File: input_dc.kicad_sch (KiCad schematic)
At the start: 24 parts

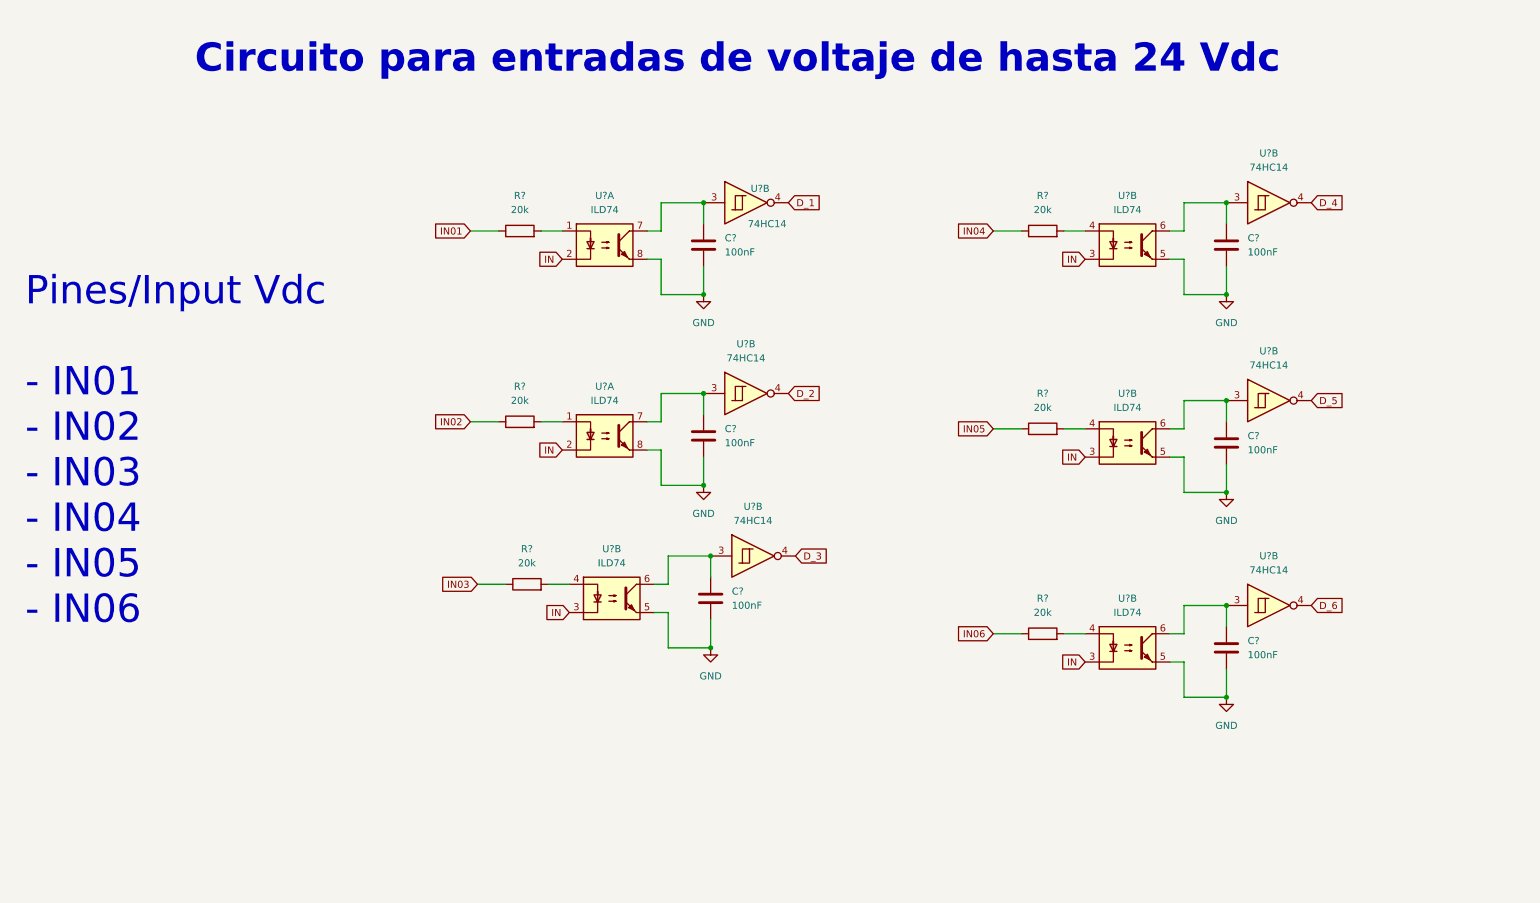
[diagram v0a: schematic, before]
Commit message: Esquema con comentarios
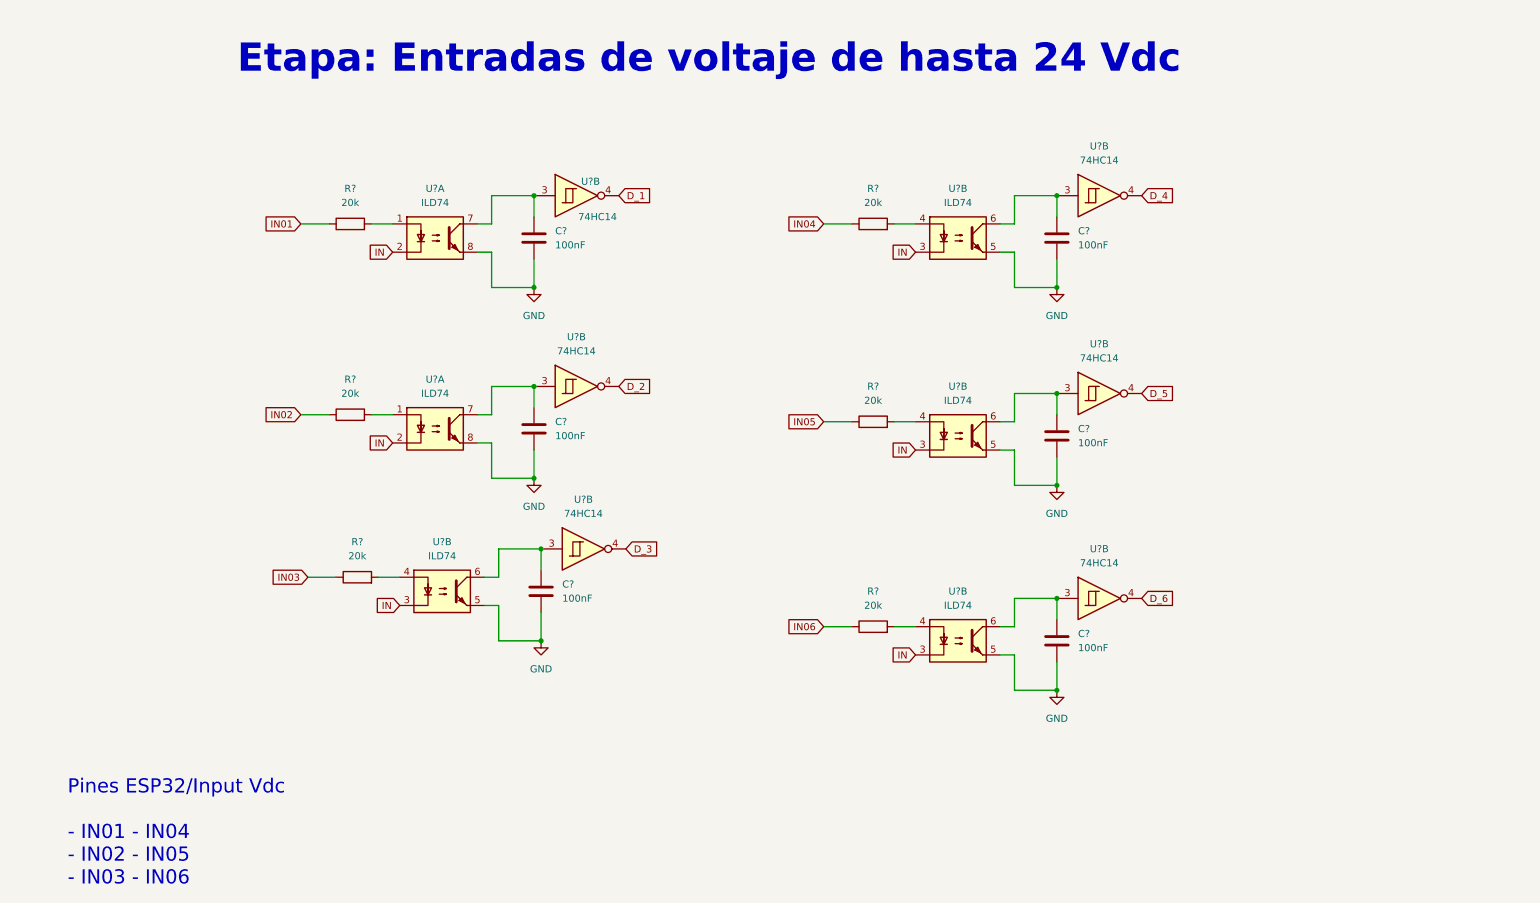
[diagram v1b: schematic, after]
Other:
- note added: "Etapa: Entradas de voltaje de hasta 24 Vdc"
- note added: "Pines ESP32/Input Vdc - IN01 - IN04 - IN02 - IN05 - IN03 - IN06"
- note removed: "Circuito para entradas de voltaje de hasta 24 Vdc"
- note removed: "Pines/Input Vdc - IN01 - IN02 - IN03 - IN04 - IN05 - IN06"
- moved on the sheet: C?, R?, U?A, U?B

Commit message: Documentación pines esp32
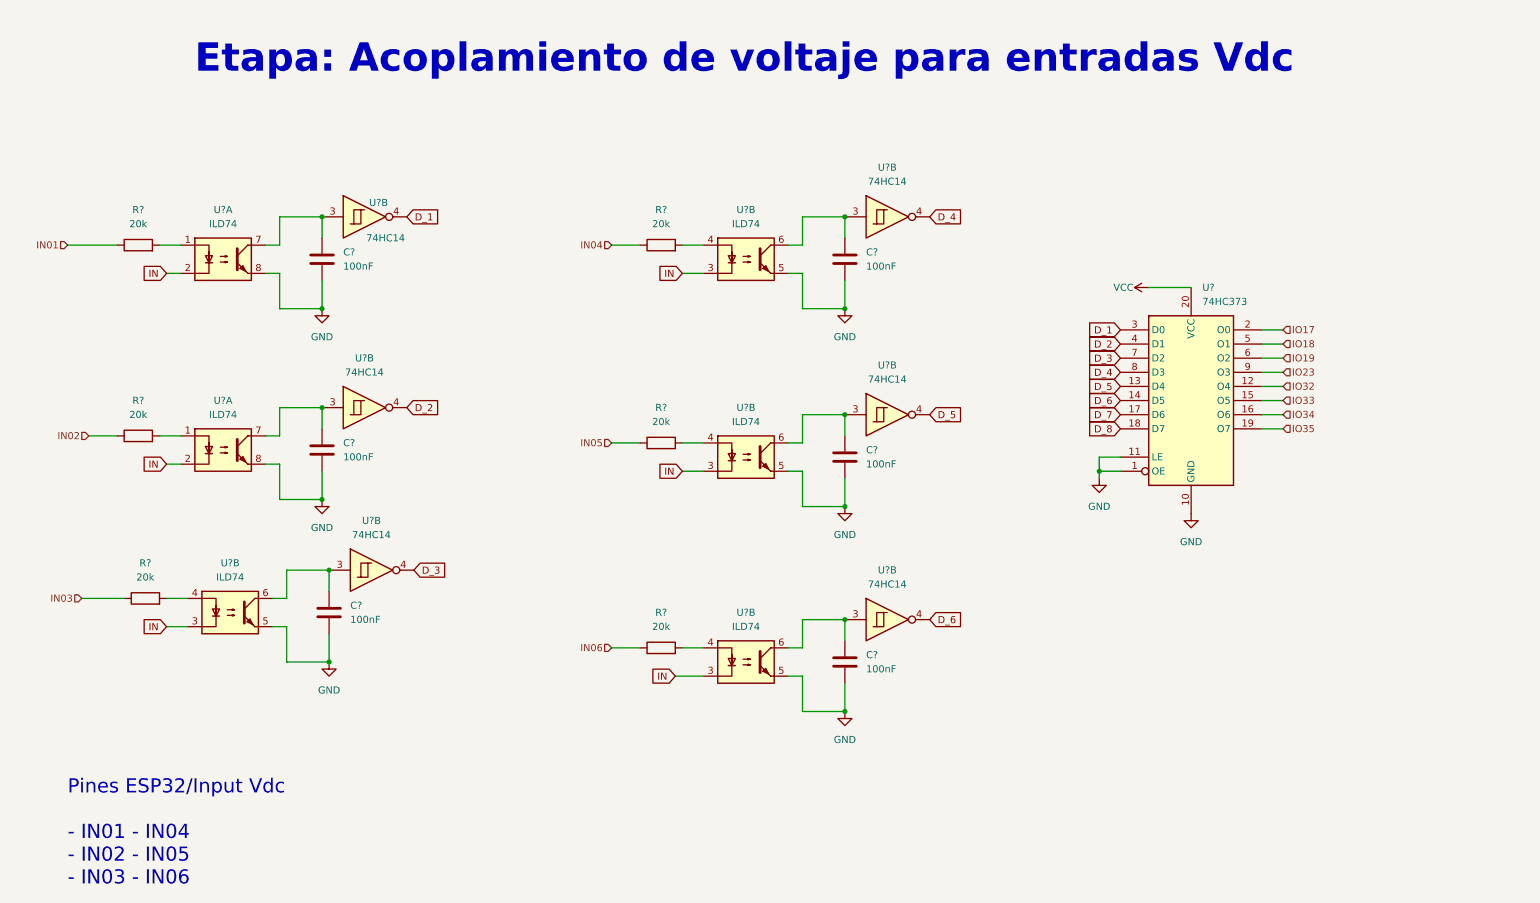
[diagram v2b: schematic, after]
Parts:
- added U?: 74HC373, Package_SO:SSOP-20_4.4x6.5mm_P0.65mm, symbol 74xx:74HC373
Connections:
- net D_1: now also U?.3 (D0)
- net D_2: now also U?.4 (D1)
- net D_3: now also U?.7 (D2)
- net D_4: now also U?.8 (D3)
- net D_5: now also U?.13 (D4)
- net D_6: now also U?.14 (D5)
- net GND: now also U?.1 (OE), U?.10 (GND), U?.11 (LE)
- new net D_7: U?.17 (D6)
- new net D_8: U?.18 (D7)
- new net IO17: U?.2 (O0)
- new net IO18: U?.5 (O1)
- new net IO19: U?.6 (O2)
- new net IO23: U?.9 (O3)
- new net IO32: U?.12 (O4)
- new net IO33: U?.15 (O5)
- new net IO34: U?.16 (O6)
- new net IO35: U?.19 (O7)
- new net VCC: U?.20 (VCC)
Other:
- note added: "Etapa: Acoplamiento de voltaje para entradas Vdc"
- note removed: "Etapa: Entradas de voltaje de hasta 24 Vdc"
- moved on the sheet: C?, R?, U?A, U?B

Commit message: add salidas separadas 1,2,3
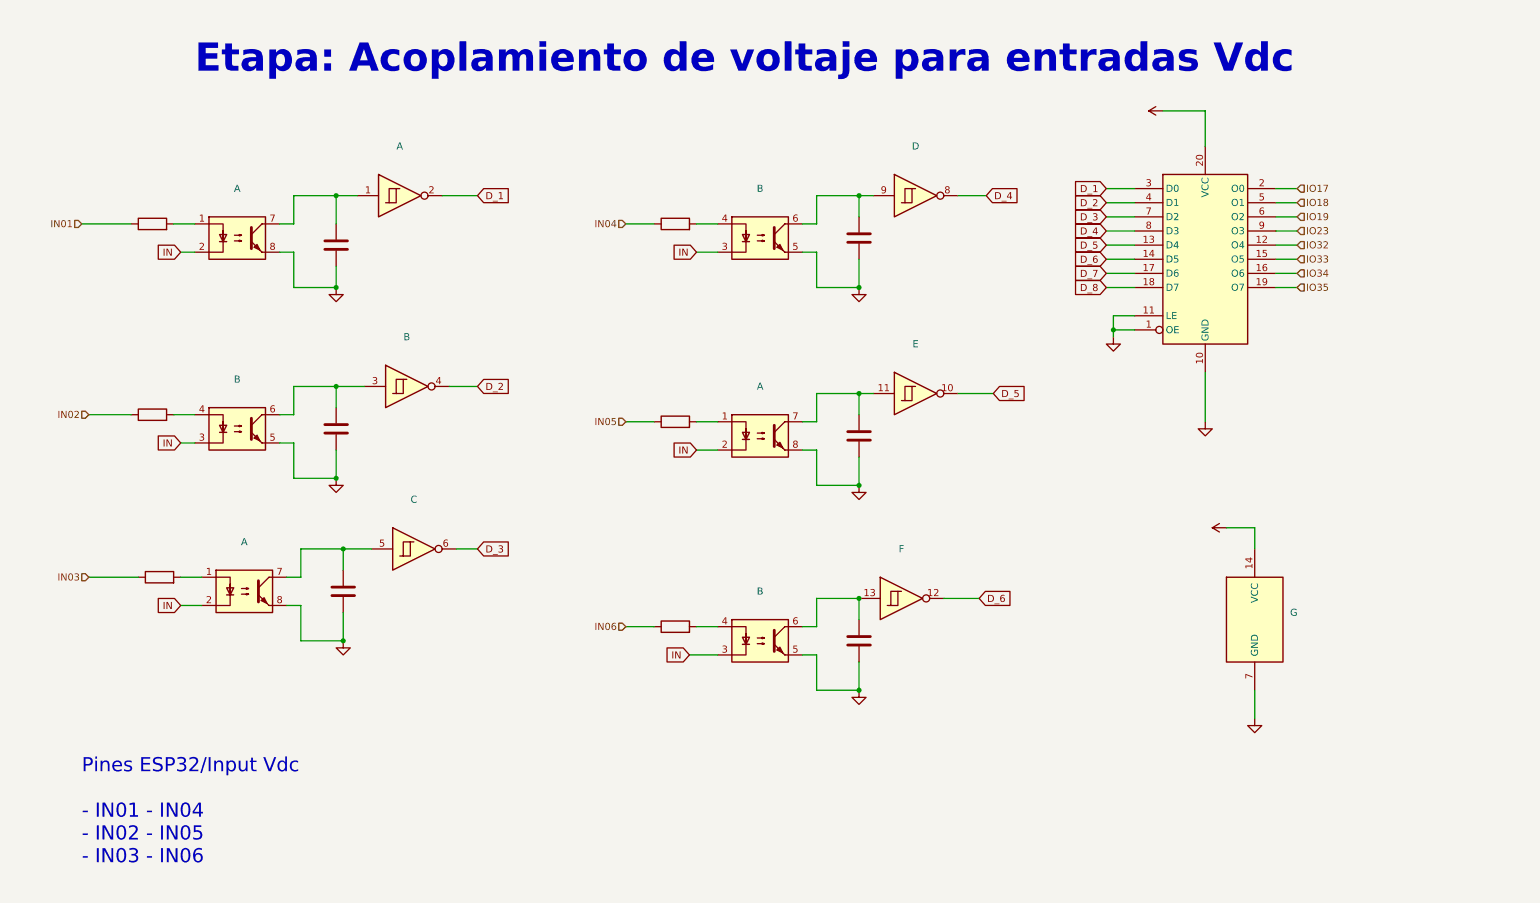
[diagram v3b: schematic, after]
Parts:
- removed U? (x6): ILD74, Package_DIP:DIP-4_W7.62mm, symbol Isolator:ILD74
- removed U? (x6): 74HC14, Package_SO:TSSOP-14_4.4x5mm_P0.65mm, symbol 74xx:74HC14
- added ? (x6): (no value), symbol Isolator:ILD74
- added ? (x7): (no value), symbol 74xx:74HC14
- ? (x6): renamed from R?; value 20k -> (none); footprint Resistor_SMD:R_0603_1608Metric_Pad0.98x0.95mm_HandSolder -> (none)
- ?: renamed from U?; value 74HC373 -> (none); footprint Package_SO:SSOP-20_4.4x6.5mm_P0.65mm -> (none)
- ? (x6): renamed from C?; value 100nF -> (none); footprint Capacitor_SMD:C_0402_1005Metric -> (none)
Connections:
- net D_1: now also ?.2
- net D_2: now also ?.4
- net D_3: now also ?.6
- net D_4: now also ?.8
- net D_5: now also ?.10
- net D_6: now also ?.12
- net GND: now also ?.5, ?.5, ?.5, ?.7 (GND), ?.8, ?.8, ?.8
- net IN: now also ?.2, ?.2, ?.2, ?.3, ?.3, ?.3
- net VCC: now also ?.14 (VCC)
- net at ?.2: now also ?.1 (x3)
- net at ?.1: now also ?.1, ?.7
- net at ?.2: now also ?.4 (x3)
- net at ?.1: now also ?.3, ?.6
- net at ?.1: now also ?.11, ?.7
- net at ?.1: now also ?.6, ?.9
- net at ?.1: now also ?.13, ?.6
- net at ?.1: now also ?.5, ?.7
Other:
- company: (none) -> INTEAMBI

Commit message: add entradas separadas
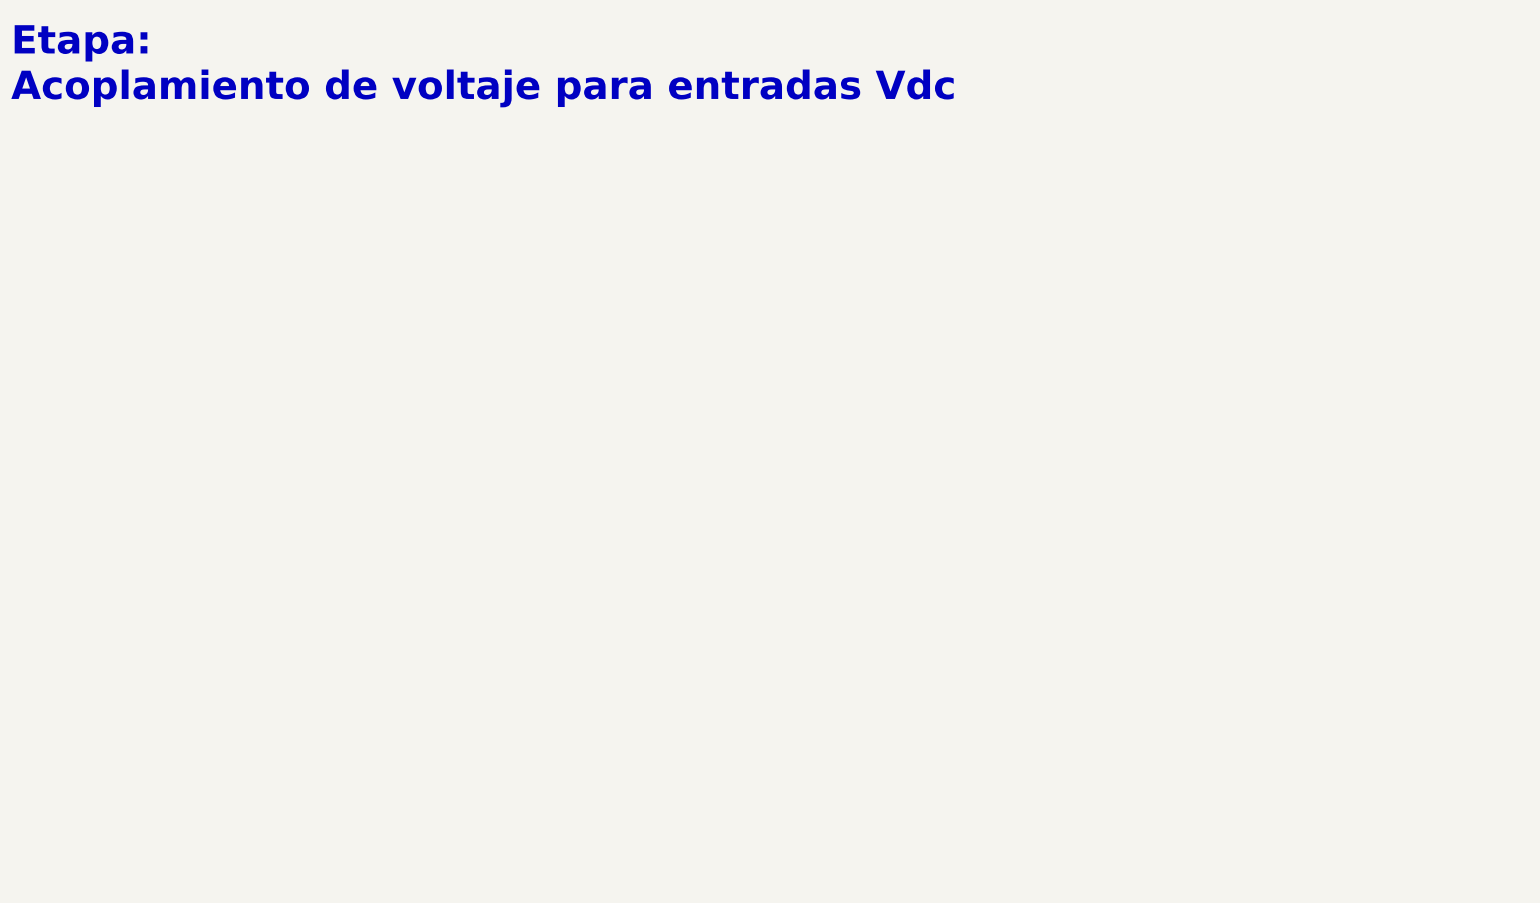
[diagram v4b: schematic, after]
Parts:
- removed ? (x6): (no value), symbol Isolator:ILD74
- removed ? (x7): (no value), symbol 74xx:74HC14
- removed ? (x6): (no value), symbol Device:R
- removed ?: (no value), symbol 74xx:74HC373
- removed ? (x6): (no value), symbol Device:C
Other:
- note removed: "Pines ESP32/Input Vdc - IN01 - IN04 - IN02 - IN05 - IN03 - IN06"
